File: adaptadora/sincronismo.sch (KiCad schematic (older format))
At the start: 60 parts, among them J13 Conn_Coaxial, J14 Conn_Coaxial, J15 Conn_Coaxial, J16 Conn_Coaxial, J17 Conn_Coaxial, J18 Conn_Coaxial, J19 Conn_Coaxial, J20 Conn_Coaxial, J21 Conn_Coaxial, U10 SN74LVC2T45DCUR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

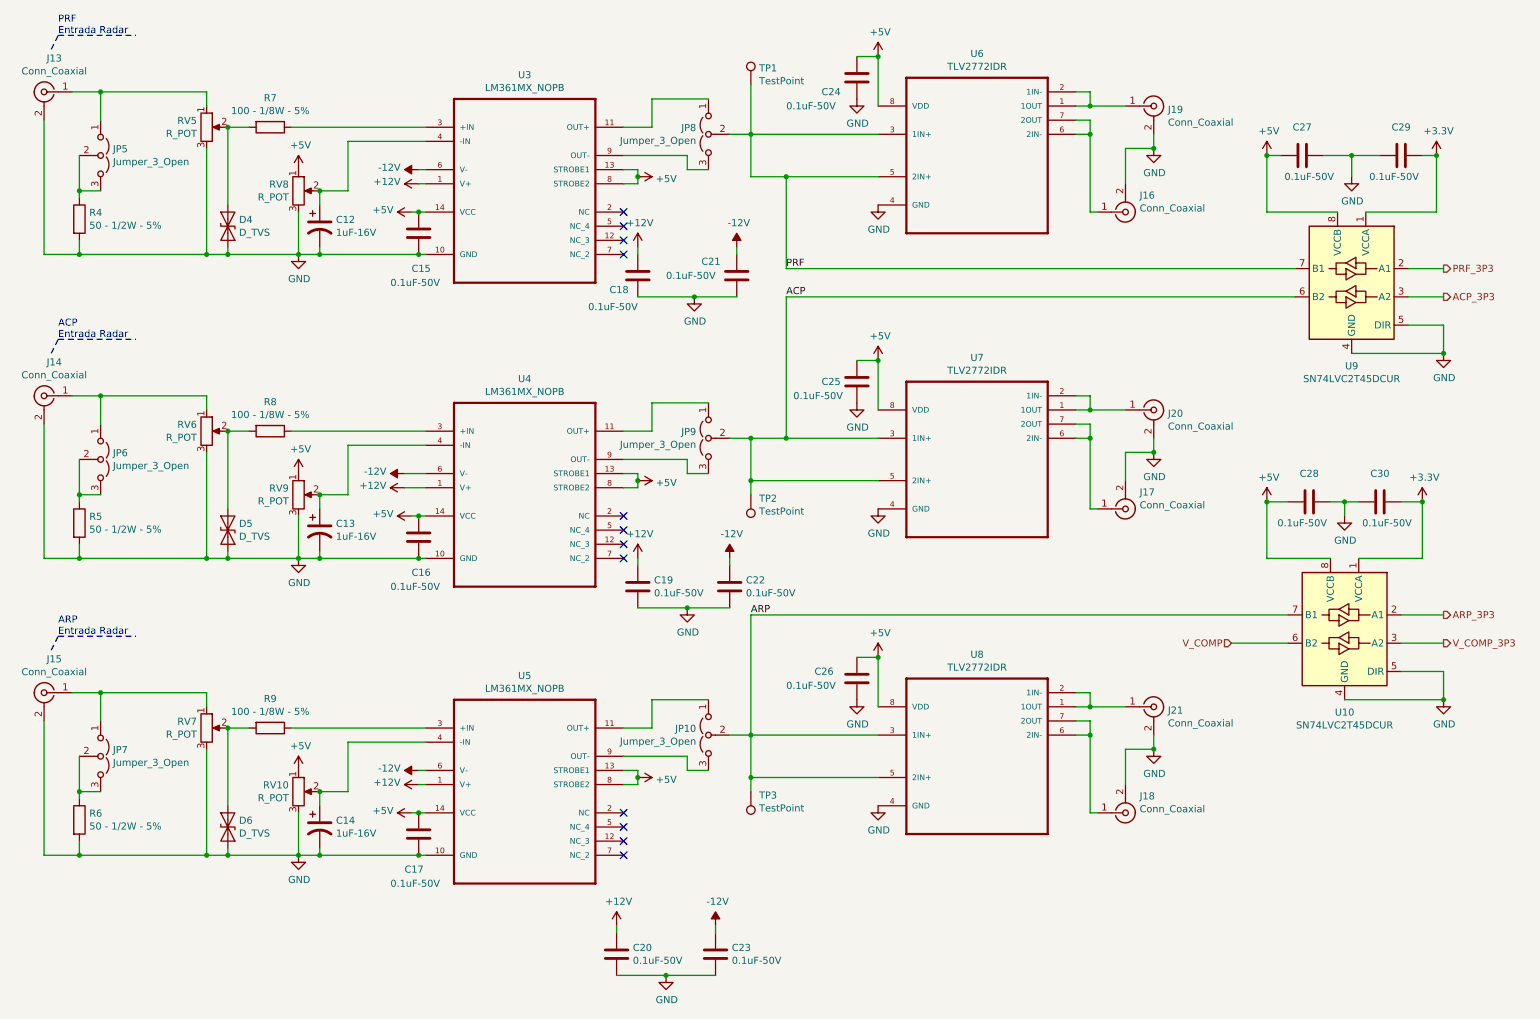
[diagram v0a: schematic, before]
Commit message: esquemático corregido por compañero
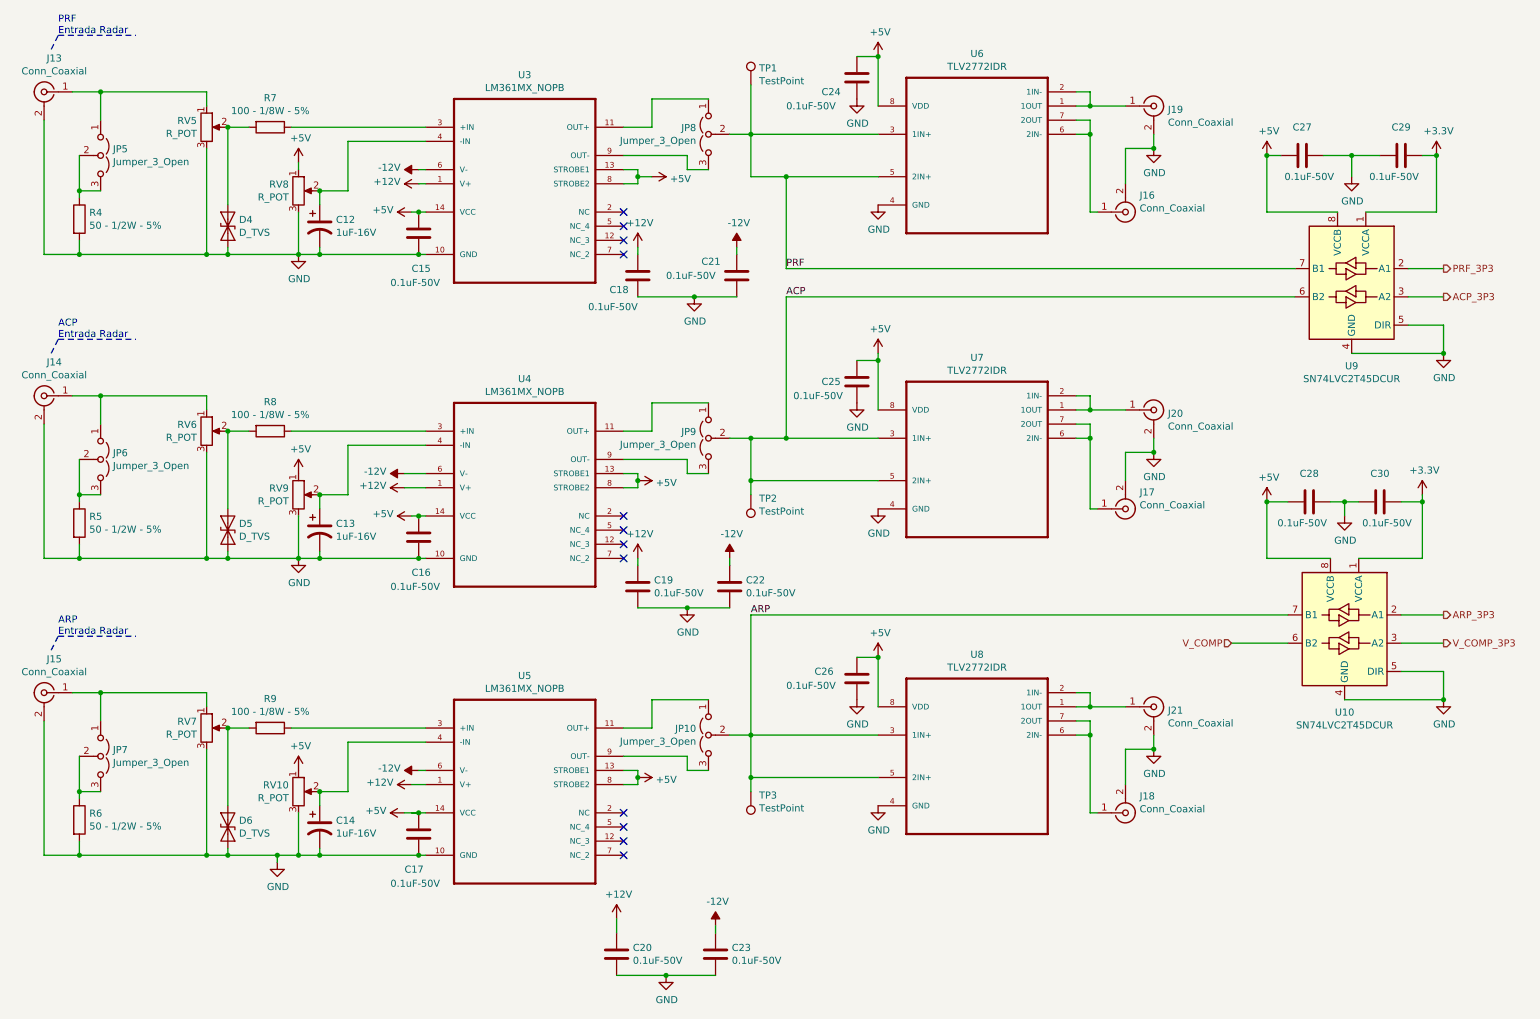
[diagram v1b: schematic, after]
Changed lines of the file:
@@
-$EndComp
-$Comp
-L Device:R_POT RV8
-U 1 1 5DA1A816
-P 2550 1750
-F 0 "RV8" H 2481 1796 50  0000 R CNN
-F 1 "R_POT" H 2481 1705 50  0000 R CNN
-F 2 "" H 2550 1750 50  0001 C CNN
-F 3 "~" H 2550 1750 50  0001 C CNN
-	1    2550 1750
-	1    0    0    -1
 $EndComp
 $Comp
@@
 Wire Wire Line
 	1000 2200 1000 2100
-$Comp
-L power:+5V #PWR027
-U 1 1 5DA49C75
-P 2550 1600
-F 0 "#PWR027" H 2550 1450 50  0001 C CNN
-F 1 "+5V" H 2565 1773 50  0000 C CNN
-F 2 "" H 2550 1600 50  0001 C CNN
-F 3 "" H 2550 1600 50  0001 C CNN
-	1    2550 1600
-	1    0    0    -1
-$EndComp
 Wire Wire Line
 	2050 1300 2050 1850
 Wire Wire Line
 	2050 2200 2050 2150
-Wire Wire Line
-	2550 1900 2550 2200
 Wire Wire Line
 	2550 2200 2050 2200
@@
 Connection ~ 2550 2200
 Wire Wire Line
-	2700 1850 2700 1750
-Wire Wire Line
 	1900 1450 1900 2200
 Connection ~ 1900 2200
@@
 Wire Wire Line
 	1900 1050 1900 1150
-Wire Wire Line
-	2700 1750 2900 1750
-Connection ~ 2700 1750
-$Comp
-L power:+5V #PWR042
-U 1 1 5DA6165B
-P 4950 1650
-F 0 "#PWR042" H 4950 1500 50  0001 C CNN
-F 1 "+5V" V 4965 1778 50  0000 L CNN
-F 2 "" H 4950 1650 50  0001 C CNN
-F 3 "" H 4950 1650 50  0001 C CNN
-	1    4950 1650
-	0    1    1    0
-$EndComp
-Wire Wire Line
-	4950 1600 4950 1650
-Wire Wire Line
-	4950 1700 4950 1650
-Connection ~ 4950 1650
-$Comp
-L power:+12V #PWR037
-U 1 1 5DA639F9
-P 3400 1700
-F 0 "#PWR037" H 3400 1550 50  0001 C CNN
-F 1 "+12V" V 3415 1828 50  0000 L CNN
-F 2 "" H 3400 1700 50  0001 C CNN
-F 3 "" H 3400 1700 50  0001 C CNN
-	1    3400 1700
-	0    -1   -1   0
-$EndComp
 $Comp
 L power:-12V #PWR036
@@
 $EndComp
 $Comp
-L power:+12V #PWR046
-U 1 1 5E259984
-P 4950 4350
-F 0 "#PWR046" H 4950 4200 50  0001 C CNN
-F 1 "+12V" H 4965 4523 50  0000 C CNN
-F 2 "" H 4950 4350 50  0001 C CNN
-F 3 "" H 4950 4350 50  0001 C CNN
-	1    4950 4350
-	1    0    0    -1
-$EndComp
-$Comp
 L power:-12V #PWR052
 U 1 1 5E25998A
@@
 L power:+5V #PWR059
 U 1 1 5E259995
-P 6650 2950
-F 0 "#PWR059" H 6650 2800 50  0001 C CNN
-F 1 "+5V" H 6665 3123 50  0000 C CNN
-F 2 "" H 6650 2950 50  0001 C CNN
-F 3 "" H 6650 2950 50  0001 C CNN
-	1    6650 2950
+P 6650 2900
+F 0 "#PWR059" H 6650 2750 50  0001 C CNN
+F 1 "+5V" H 6665 3073 50  0000 C CNN
+F 2 "" H 6650 2900 50  0001 C CNN
+F 3 "" H 6650 2900 50  0001 C CNN
+	1    6650 2900
 	1    0    0    -1
 $EndComp
@@
 	5750 3800 6650 3800
 Connection ~ 8150 3500
-$Comp
-L power:GND #PWR064
-U 1 1 5E2599BF
-P 8600 3600
-F 0 "#PWR064" H 8600 3350 50  0001 C CNN
-F 1 "GND" H 8605 3427 50  0000 C CNN
-F 2 "" H 8600 3600 50  0001 C CNN
-F 3 "" H 8600 3600 50  0001 C CNN
-	1    8600 3600
-	1    0    0    -1
-$EndComp
 Wire Wire Line
 	8600 3500 8600 3600
@@
 Wire Wire Line
 	8400 3600 8600 3600
-Connection ~ 8600 3600
-$Comp
-L power:GND #PWR060
-U 1 1 5E2599C9
-P 6650 4000
-F 0 "#PWR060" H 6650 3750 50  0001 C CNN
-F 1 "GND" H 6655 3827 50  0000 C CNN
-F 2 "" H 6650 4000 50  0001 C CNN
-F 3 "" H 6650 4000 50  0001 C CNN
-	1    6650 4000
-	1    0    0    -1
-$EndComp
 $Comp
 L power:GND #PWR055
@@
 $EndComp
 Wire Wire Line
-	6500 2950 6650 2950
-Wire Wire Line
-	6650 2950 6650 3300
-Connection ~ 6650 2950
+	6650 2900 6650 2950
 $Comp
 L Connector:Conn_Coaxial J15
@@
 	2550 6150 2550 6450
 Wire Wire Line
-	2550 6450 2050 6450
+	2550 6450 2400 6450
 Connection ~ 2050 6450
 Connection ~ 2550 6450
@@
 L power:+12V #PWR041
 U 1 1 5E26D5A3
-P 3400 5950
-F 0 "#PWR041" H 3400 5800 50  0001 C CNN
-F 1 "+12V" V 3415 6078 50  0000 L CNN
-F 2 "" H 3400 5950 50  0001 C CNN
-F 3 "" H 3400 5950 50  0001 C CNN
-	1    3400 5950
+P 3350 5950
+F 0 "#PWR041" H 3350 5800 50  0001 C CNN
+F 1 "+12V" V 3365 6078 50  0000 L CNN
+F 2 "" H 3350 5950 50  0001 C CNN
+F 3 "" H 3350 5950 50  0001 C CNN
+	1    3350 5950
 	0    -1   -1   0
 $EndComp
@@
 	1    3400 6300
 	-1   0    0    1
-$EndComp
-$Comp
-L power:+5V #PWR035
-U 1 1 5E26D5BD
-P 3350 6150
-F 0 "#PWR035" H 3350 6000 50  0001 C CNN
-F 1 "+5V" V 3365 6278 50  0000 L CNN
-F 2 "" H 3350 6150 50  0001 C CNN
-F 3 "" H 3350 6150 50  0001 C CNN
-	1    3350 6150
-	0    -1   -1   0
 $EndComp
 Wire Wire Line
@@
 L power:GND #PWR032
 U 1 1 5E26D5CF
-P 2550 6450
-F 0 "#PWR032" H 2550 6200 50  0001 C CNN
-F 1 "GND" H 2555 6277 50  0000 C CNN
-F 2 "" H 2550 6450 50  0001 C CNN
-F 3 "" H 2550 6450 50  0001 C CNN
-	1    2550 6450
+P 2400 6500
+F 0 "#PWR032" H 2400 6250 50  0001 C CNN
+F 1 "GND" H 2405 6327 50  0000 C CNN
+F 2 "" H 2400 6500 50  0001 C CNN
+F 3 "" H 2400 6500 50  0001 C CNN
+	1    2400 6500
 	1    0    0    -1
 $EndComp
@@
 Wire Wire Line
 	4850 5950 4950 5950
-Wire Wire Line
-	3350 6150 3400 6150
 Wire Wire Line
 	3450 6150 3400 6150
@@
 Wire Wire Line
 	3400 5850 3450 5850
-Wire Wire Line
-	3400 5950 3450 5950
 Wire Wire Line
 	3450 5650 2900 5650
@@
 F 3 "" H 5150 7300 50  0001 C CNN
 	1    5150 7300
-	1    0    0    -1
-$EndComp
-$Comp
-L power:+12V #PWR047
-U 1 1 5E26D60B
-P 4800 6950
-F 0 "#PWR047" H 4800 6800 50  0001 C CNN
-F 1 "+12V" H 4815 7123 50  0000 C CNN
-F 2 "" H 4800 6950 50  0001 C CNN
-F 3 "" H 4800 6950 50  0001 C CNN
-	1    4800 6950
 	1    0    0    -1
 $EndComp
@@
 $EndComp
 $Comp
-L power:+5V #PWR067
-U 1 1 5E27ED1E
-P 9400 3950
-F 0 "#PWR067" H 9400 3800 50  0001 C CNN
-F 1 "+5V" H 9415 4123 50  0000 C CNN
-F 2 "" H 9400 3950 50  0001 C CNN
-F 3 "" H 9400 3950 50  0001 C CNN
-	1    9400 3950
-	1    0    0    -1
-$EndComp
-$Comp
-L power:+3.3V #PWR072
-U 1 1 5E27ED24
-P 10500 3950
-F 0 "#PWR072" H 10500 3800 50  0001 C CNN
-F 1 "+3.3V" H 10515 4123 50  0000 C CNN
-F 2 "" H 10500 3950 50  0001 C CNN
-F 3 "" H 10500 3950 50  0001 C CNN
-	1    10500 3950
-	1    0    0    -1
-$EndComp
-$Comp
 L power:GND #PWR069
 U 1 1 5E27ED2A
@@
 Wire Wire Line
 	9400 4350 9850 4350
-Connection ~ 9400 3950
 Wire Wire Line
 	10050 3950 9950 3950
@@
 	5150 7300 5500 7300
 Connection ~ 5150 7300
-Wire Wire Line
-	4800 6950 4800 7000
 Wire Wire Line
 	5500 6950 5500 7000
@@
 NoConn ~ 4850 2000
 NoConn ~ 4850 1900
+Wire Wire Line
+	6500 2950 6650 2950
+Connection ~ 6650 2950
+Wire Wire Line
+	6650 2950 6650 3300
+Wire Wire Line
+	4950 1600 4950 1650
+Wire Wire Line
+	5050 1650 4950 1650
+Connection ~ 4950 1650
+Wire Wire Line
+	4950 1650 4950 1700
+Wire Wire Line
+	4800 6900 4800 7000
+Wire Wire Line
+	2550 1900 2550 2200
+Connection ~ 2700 1750
+Wire Wire Line
+	2700 1750 2900 1750
+Wire Wire Line
+	2700 1850 2700 1750
+$Comp
+L Device:R_POT RV8
+U 1 1 5DA1A816
+P 2550 1750
+F 0 "RV8" H 2481 1796 50  0000 R CNN
+F 1 "R_POT" H 2481 1705 50  0000 R CNN
+F 2 "" H 2550 1750 50  0001 C CNN
+F 3 "~" H 2550 1750 50  0001 C CNN
+	1    2550 1750
+	1    0    0    -1
+$EndComp
+$Comp
+L power:+5V #PWR027
+U 1 1 5DA49C75
+P 2550 1550
+F 0 "#PWR027" H 2550 1400 50  0001 C CNN
+F 1 "+5V" H 2565 1723 50  0000 C CNN
+F 2 "" H 2550 1550 50  0001 C CNN
+F 3 "" H 2550 1550 50  0001 C CNN
+	1    2550 1550
+	1    0    0    -1
+$EndComp
+Wire Wire Line
+	2550 1550 2550 1600
+Wire Wire Line
+	3350 6150 3400 6150
+Wire Wire Line
+	3350 5950 3450 5950
+Wire Wire Line
+	3300 6150 3400 6150
+Wire Wire Line
+	10500 3900 10500 3950
+Wire Wire Line
+	2400 6500 2400 6450
+Connection ~ 2400 6450
+Wire Wire Line
+	2400 6450 2050 6450
+$Comp
+L power:+5V #PWR0103
+U 1 1 5E358A06
+P 3300 6150
+F 0 "#PWR0103" H 3300 6000 50  0001 C CNN
+F 1 "+5V" V 3315 6278 50  0000 L CNN
+F 2 "" H 3300 6150 50  0001 C CNN
+F 3 "" H 3300 6150 50  0001 C CNN
+	1    3300 6150
+	0    -1   -1   0
+$EndComp
+$Comp
+L power:+3.3V #PWR0106
+U 1 1 5E379E24
+P 10500 3900
+F 0 "#PWR0106" H 10500 3750 50  0001 C CNN
+F 1 "+3.3V" H 10515 4073 50  0000 C CNN
+F 2 "" H 10500 3900 50  0001 C CNN
+F 3 "" H 10500 3900 50  0001 C CNN
+	1    10500 3900
+	1    0    0    -1
+$EndComp
+$Comp
+L power:GND #PWR0108
+U 1 1 5E37BE4D
+P 6650 4000
+F 0 "#PWR0108" H 6650 3750 50  0001 C CNN
+F 1 "GND" H 6655 3827 50  0000 C CNN
+F 2 "" H 6650 4000 50  0001 C CNN
+F 3 "" H 6650 4000 50  0001 C CNN
+	1    6650 4000
+	1    0    0    -1
+$EndComp
+$Comp
+L power:+5V #PWR0113
+U 1 1 5E388521
+P 9400 3950
+F 0 "#PWR0113" H 9400 3800 50  0001 C CNN
+F 1 "+5V" H 9415 4123 50  0000 C CNN
+F 2 "" H 9400 3950 50  0001 C CNN
+F 3 "" H 9400 3950 50  0001 C CNN
+	1    9400 3950
+	1    0    0    -1
+$EndComp
+Connection ~ 9400 3950
+$Comp
+L power:+5V #PWR0115
+U 1 1 5E393459
+P 5050 1650
+F 0 "#PWR0115" H 5050 1500 50  0001 C CNN
+F 1 "+5V" V 5065 1778 50  0000 L CNN
+F 2 "" H 5050 1650 50  0001 C CNN
+F 3 "" H 5050 1650 50  0001 C CNN
+	1    5050 1650
+	0    1    1    0
+$EndComp
+$Comp
+L power:+12V #PWR0118
+U 1 1 5E3C5964
+P 3400 1700
+F 0 "#PWR0118" H 3400 1550 50  0001 C CNN
+F 1 "+12V" V 3415 1828 50  0000 L CNN
+F 2 "" H 3400 1700 50  0001 C CNN
+F 3 "" H 3400 1700 50  0001 C CNN
+	1    3400 1700
+	0    -1   -1   0
+$EndComp
+$Comp
+L power:+12V #PWR0119
+U 1 1 5E3D7809
+P 4800 6900
+F 0 "#PWR0119" H 4800 6750 50  0001 C CNN
+F 1 "+12V" H 4815 7073 50  0000 C CNN
+F 2 "" H 4800 6900 50  0001 C CNN
+F 3 "" H 4800 6900 50  0001 C CNN
+	1    4800 6900
+	1    0    0    -1
+$EndComp
+$Comp
+L power:+12V #PWR0120
+U 1 1 5E3D862D
+P 4950 4350
+F 0 "#PWR0120" H 4950 4200 50  0001 C CNN
+F 1 "+12V" H 4965 4523 50  0000 C CNN
+F 2 "" H 4950 4350 50  0001 C CNN
+F 3 "" H 4950 4350 50  0001 C CNN
+	1    4950 4350
+	1    0    0    -1
+$EndComp
+Connection ~ 8600 3600
+$Comp
+L power:GND #PWR064
+U 1 1 5E2599BF
+P 8600 3600
+F 0 "#PWR064" H 8600 3350 50  0001 C CNN
+F 1 "GND" H 8605 3427 50  0000 C CNN
+F 2 "" H 8600 3600 50  0001 C CNN
+F 3 "" H 8600 3600 50  0001 C CNN
+	1    8600 3600
+	1    0    0    -1
+$EndComp
 $EndSCHEMATC
